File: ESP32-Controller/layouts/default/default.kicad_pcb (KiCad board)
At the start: 2 copper layers, 50 x 30 mm, 25 parts

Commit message: PoE Improvements
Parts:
- added C10: 10µF ±10%, Samsung_Electro_Mechanics_CL10A106KP8NNNC:C0603, F.Cu at (126.8, 101.1)
- added C11: 22µF ±20%, Samsung_Electro_Mechanics_CL10A226MQ8NRNC:C0603, F.Cu at (116.4, 95.5)
- added R7: 5.1kΩ ±1%, UNI_ROYAL_0402WGF5101TCE:R0402, F.Cu at (118.8, 92.4)
- added R8: 5.1kΩ ±1%, UNI_ROYAL_0402WGF5101TCE:R0402, F.Cu at (118.2, 88.3)
- added U2: , Advanced_Monolithic_Systems_AMS1117_3_3:SOT-223-3_L6.5-W3.4-P2.30-LS7.0-BR, F.Cu at (120.8, 100.6)
- R2: value 40.2kΩ ±1% -> 22kΩ ±1%; footprint UNI_ROYAL_0603WAF4022T5E:R0603 -> UNI_ROYAL_0603WAF2202T5E:R0603
- USB1: footprint Hanbo_Electronic_MC_401L68_Z09:USB-C-SMD_MC-401L68-Z09 -> Shenzhen_Kinghelm_Elec_KH_TYPE_C_16P:USB-C-SMD_KH-TYPE-C-16P
- moved USB1 8.31 mm to (123.4, 90.3), turned to 90 degrees
- moved D1 8.27 mm to (111.2, 85.1)
- moved C1 7.40 mm to (105.4, 101.0), turned to -90 degrees
- moved C2 4.80 mm to (98.8, 100.5), turned to 90 degrees
- moved 15V-25V DC 4.12 mm to (117.4, 82.6)
- moved C3 3.89 mm to (96.6, 100.5), turned to 90 degrees
- moved U1 0.30 mm to (102.2, 101.0), turned to 180 degrees
- renumbered SW1 to BOOT, SW2 to RESET
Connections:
- net A renamed BOOT
- net en_cap-power-hv renamed RESET
- D1 pad 1: V+ -> 5V
- L1 pad 2: 3V3 -> 5V
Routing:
- net 5V: track 0.00 -> 41.1 mm, vias 0 -> 3
- net V+: track 93.7 -> 62.6 mm
- net 3V3: track 56.4 -> 71.0 mm, vias 2 -> 0
- net lv: track 19.9 -> 8.04 mm
- net USB_Vin: track 12.9 -> 17.0 mm
- net GND: track 0.00 -> 3.08 mm, vias 10 -> 11
- net B5: track 0.00 -> 2.47 mm
- net A5: track 0.00 -> 2.38 mm
- net bst_cap-power-hv: track 3.40 -> 2.12 mm
- net fb_cap-power-lv: track 15.3 -> 16.6 mm, vias 0 -> 2
- net BOOT: track 12.7 -> 13.7 mm
- net A7: track 13.2 -> 13.8 mm
- net pwm_warm: vias 1 -> 2
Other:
- board size 50 x 30 mm -> 53.8 x 30 mm

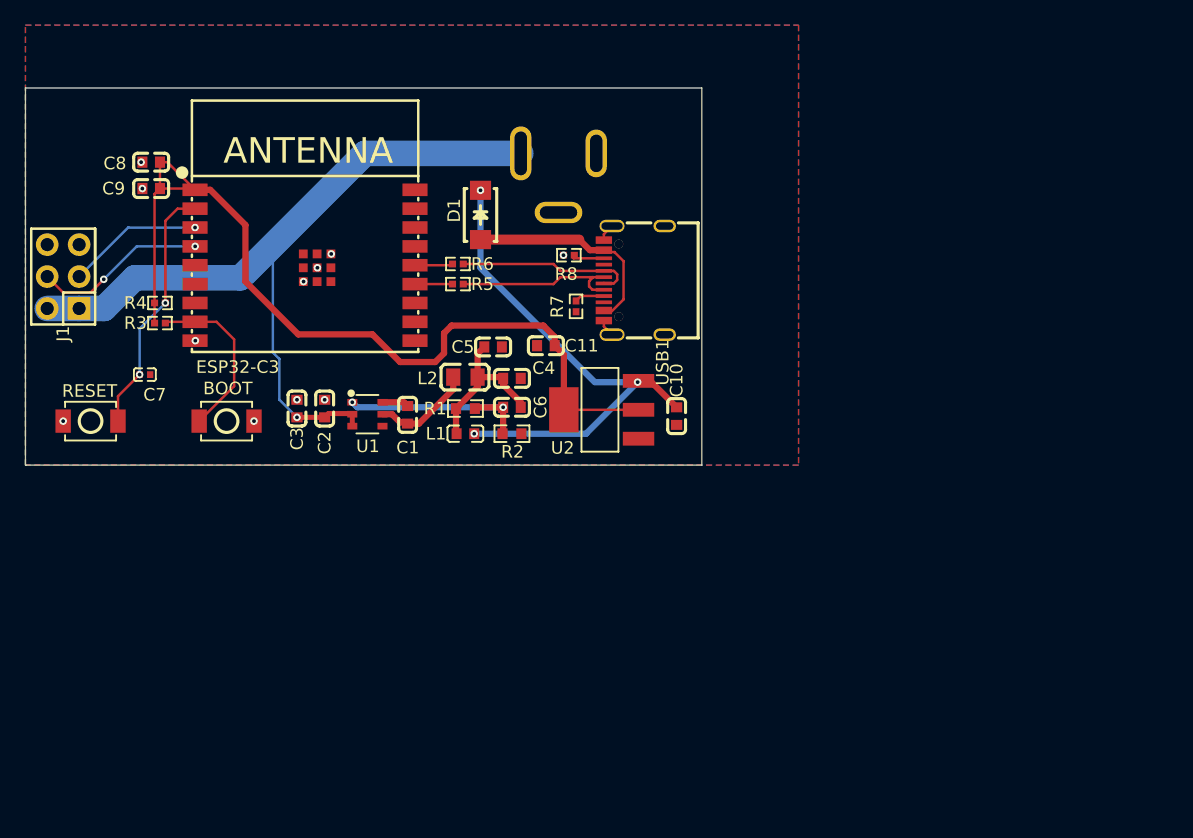
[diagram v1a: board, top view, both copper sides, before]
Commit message: ESP32 New Buck & Header Updates
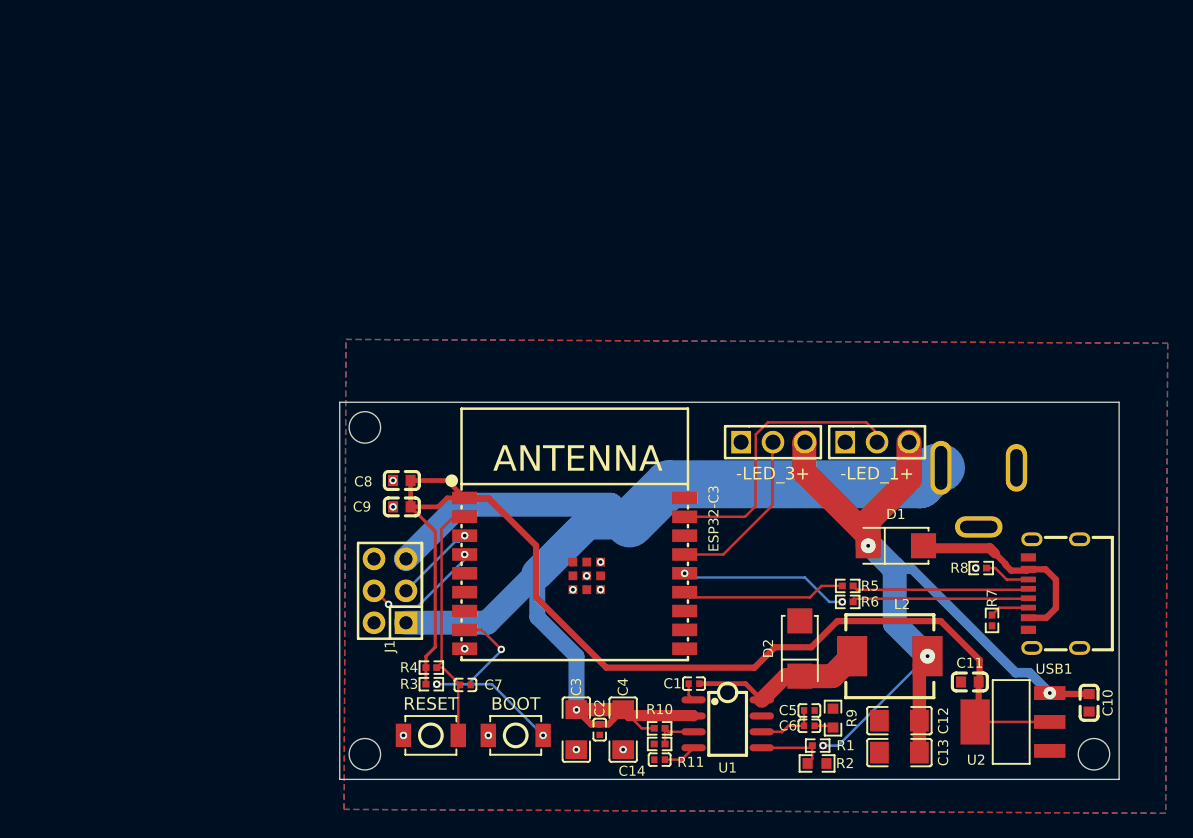
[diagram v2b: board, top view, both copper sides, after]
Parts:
- removed L1: , Murata_Electronics_BLM18PG121SN1D:L0603
- added -LED_1+: , BOOMELE_2_54_1_3P:HDR-TH_3P-P2.54-V-M-1, F.Cu at (142.7, 103.2)
- added -LED_3+: , BOOMELE_2_54_1_3P:HDR-TH_3P-P2.54-V-M-1, F.Cu at (134.5, 103.2)
- added C12: 47µF ±20%, Samsung_Electro_Mechanics_CL31A476MPHNNNE:C1206, F.Cu at (144.5, 125.3)
- added C13: 47µF ±20%, Samsung_Electro_Mechanics_CL31A476MPHNNNE:C1206, F.Cu at (144.5, 127.9)
- added C14: 10nF ±10%, Samsung_Electro_Mechanics_CL05B103KB5NNNC:C0402, F.Cu at (125.4, 128.4)
- added D2: Vf {ℝ+}V, MDD_Microdiode_Electronics_SS34:SMA_L4.3-W2.6-LS5.2-RD, F.Cu at (136.6, 119.6)
- added R10: 330kΩ ±1%, UNI_ROYAL_0402WGF3303TCE:R0402, F.Cu at (125.4, 125.9)
- added R11: 68kΩ ±1%, UNI_ROYAL_0402WGF6802TCE:R0402, F.Cu at (125.4, 127.2)
- added R9: 30kΩ ±1%, UNI_ROYAL_0603WAF3002T5E:R0603, F.Cu at (139.2, 125.1)
- C1: footprint YAGEO_CC0603KRX7R9BB104:C0603 -> Samsung_Electro_Mechanics_CL05B104KO5NNNC:C0402
- C10, C8: value 10µF ±10% -> 10µF ±20%
- C2: value 100nF ±10% -> 10nF ±10%; footprint YAGEO_CC0603KRX7R9BB104:C0603 -> Samsung_Electro_Mechanics_CL05B103KB5NNNC:C0402
- C3: value 10µF ±10% -> 4.7µF ±20%; footprint Samsung_Electro_Mechanics_CL10A106KP8NNNC:C0603 -> FH_1206B475K500NT:C1206
- C4: value 22µF ±20% -> 4.7µF ±20%; footprint Samsung_Electro_Mechanics_CL10A226MQ8NRNC:C0603 -> FH_1206B475K500NT:C1206
- C5: value 22µF ±20% -> 47pF ±5%; footprint Samsung_Electro_Mechanics_CL10A226MQ8NRNC:C0603 -> FH_0402CG470J500NT:C0402
- C6: value 47pF ±5% -> 1nF ±10%; footprint Samsung_Electro_Mechanics_CL10C470JB8NNNC:C0603 -> FH_0402B102K500NT:C0402
- C7: value 1µF ±10% -> 1µF ±20%
- C9: value 100nF ±10% -> 100nF ±20%
- D1: footprint MDD_Microdiode_Electronics_SS14:SMA_L4.2-W2.6-LS5.0-RD_1 -> MDD_Microdiode_Electronics_SS34:SMA_L4.3-W2.6-LS5.2-RD
- L2: footprint microgate_MGFL2012F6R8MT_LF:L0805 -> TECHFUSE_SL0630_6R8M:IND-SMD_L7.0-W6.6
- R1: value 120kΩ ±1% -> {ℝ+}Ω; footprint UNI_ROYAL_0603WAF1203T5E:R0603 -> UNI_ROYAL_0402WGF1002TCE:R0402
- R2: value 22kΩ ±1% -> {ℝ+}Ω; footprint UNI_ROYAL_0603WAF2202T5E:R0603 -> UNI_ROYAL_0603WAF1801T5E:R0603
- R3, R4: value 10kΩ ±1% -> 10kΩ ±5%
- R5, R6: value 22Ω ±1% -> 22Ω ±5%
- R7, R8: value 5.1kΩ ±1% -> 5.1kΩ ±5%
- U1: footprint Diodes_Incorporated_AP63301WU_7:TSOT-23-6_L2.9-W1.6-P0.95-LS2.8-BR -> Texas_Instruments_TPS54331DR:SOIC-8_L5.0-W4.0-P1.27-LS6.0-BL
- USB1: footprint Shenzhen_Kinghelm_Elec_KH_TYPE_C_16P:USB-C-SMD_KH-TYPE-C-16P -> Hanbo_Electronic_MC_403L68_Z20:USB-C-SMD_MC-403L68-Z20
- moved C11 43.0 mm to (150.1, 122.3)
- moved D1 42.2 mm to (144.2, 111.4), turned to 0 degrees
- moved 15V-25V DC 41.8 mm to (150.8, 107.6)
- moved USB1 41.7 mm to (156.8, 115.2)
- moved R7 41.5 mm to (151.9, 117.4)
- moved R8 41.2 mm to (151.0, 113.2)
- moved U2 41.1 mm to (153.5, 125.4)
- moved R6 41.0 mm to (140.4, 115.9)
- moved L2 40.4 mm to (143.8, 120.2)
- moved C10 40.0 mm to (159.6, 123.9)
- moved R5 39.2 mm to (140.4, 114.6)
- moved R1 38.8 mm to (138.0, 127.3), turned to 180 degrees
- moved C5 38.3 mm to (137.4, 124.5)
- moved U1 37.8 mm to (130.9, 125.6), turned to -90 degrees
- moved RESET 36.8 mm to (107.2, 126.5)
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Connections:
- net A5 renamed CC1
- net B5 renamed CC2
- C1 pad 1: bst_cap-power-hv -> hv
- C1 pad 2: lv -> cathode
- C4 pad 1: hv -> V+
- C5 pad 1: hv -> comp_c2-power-hv
- C6 pad 1: hv -> comp_c2-power-hv
- C6 pad 2: fb_cap-power-lv -> lv
- D1 pad 2: USB_Vin -> vUSB
- ESP32-C3 pad 15: 15 -> 2-1
- ESP32-C3 pad 17: 17 -> 2
- J1 pad 2: V+ -> GND
- J1 pad 5: GND -> V+
- L2 pad 1: lv -> cathode
- L2 pad 2: hv -> 5V
- R1 pad 1: hv -> 5V
- R1 pad 2: fb_cap-power-lv -> VSENSE
- R2 pad 1: fb_cap-power-lv -> VSENSE
- R5 pad 1: A7 -> usb_n
- R6 pad 1: A6 -> usb_p
- U1 pad 1: fb_cap-power-lv -> hv
- U1 pad 3: V+ -> EN
- U1 pad 4: GND -> ss_cap-power-hv
- U1 pad 5: lv -> VSENSE
- U1 pad 6: bst_cap-power-hv -> comp_c2-power-hv
- USB1 pad A6: A6 -> usb_p
- USB1 pad A7: A7 -> usb_n
- USB1 pad B4: USB_Vin -> vUSB
- USB1 pad B9: USB_Vin -> vUSB
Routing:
- net V+: track 62.6 -> 97.3 mm
- net 5V: track 41.1 -> 68.7 mm, vias 3 -> 4
- net 2: track 0.00 -> 22.0 mm
- net 3V3: track 71.0 -> 89.6 mm
- net USB_Vin: track 17.0 -> 0.00 mm
- net vUSB: track 0.00 -> 16.8 mm
- net fb_cap-power-lv: track 16.6 -> 0.00 mm, vias 2 -> 0
- net 2-1: track 0.00 -> 14.4 mm
- net A6: track 14.2 -> 0.00 mm
- net cathode: track 0.00 -> 14.1 mm
- net usb_n: track 0.00 -> 14.1 mm
- net usb_p: track 0.00 -> 14.0 mm
- net A7: track 13.8 -> 0.00 mm
- net hv: track 12.8 -> 1.45 mm
- net 14: track 3.02 -> 13.7 mm, vias 0 -> 2
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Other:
- board size 53.8 x 30 mm -> 62 x 30 mm

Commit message: Header & Silkscreen Updates
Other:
- board text added: "ESP32 LED Panel Controller v1.1.0 - May 2026"

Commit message: Basic layout tweaks
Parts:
- moved -LED_3+ 2.22 mm to (132.2, 103.2)
- moved -LED_1+ 0.50 mm to (142.2, 103.2)
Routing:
- net 2-1: track 14.4 -> 12.7 mm
- net 5V: track 68.7 -> 70.1 mm
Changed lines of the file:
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@@
 	(footprint "BOOMELE_2_54_1_3P:HDR-TH_3P-P2.54-V-M-1"
 		(layer "F.Cu")
-		(at 142.748 103.1748)
+		(at 142.25 103.1748)
 		(property "Reference" "-LED_1+"
 			(at 0 2.5 0)
@@
 	(footprint "BOOMELE_2_54_1_3P:HDR-TH_3P-P2.54-V-M-1"
 		(layer "F.Cu")
-		(at 134.4676 103.1748)
+		(at 132.25 103.1748)
 		(property "Reference" "-LED_3+"
 			(at 0 2.5 0)
@@
 	)
 	(segment
-		(start 133.096 108.2548)
-		(end 133.096 102.5652)
+		(start 127.4416 109.1096)
+		(end 129.3904 109.1096)
 		(width 0.2)
 		(layer "F.Cu")
@@
 	)
 	(segment
-		(start 133.096 102.5652)
-		(end 134.0612 101.6)
+		(start 141.8844 101.6)
+		(end 142.25 101.9656)
 		(width 0.2)
 		(layer "F.Cu")
@@
 	)
 	(segment
-		(start 134.0612 101.6)
+		(start 129.3904 109.1096)
+		(end 131 107.5)
+		(width 0.2)
+		(layer "F.Cu")
+		(net 30)
+	)
+	(segment
+		(start 131.9 101.6)
 		(end 141.8844 101.6)
 		(width 0.2)
@@
 	)
 	(segment
-		(start 141.8844 101.6)
-		(end 142.6972 102.4128)
+		(start 131 102.5)
+		(end 131.9 101.6)
 		(width 0.2)
 		(layer "F.Cu")
@@
 	)
 	(segment
-		(start 127.4416 109.1096)
-		(end 132.2412 109.1096)
+		(start 131 107.5)
+		(end 131 102.5)
 		(width 0.2)
 		(layer "F.Cu")
@@
 	)
 	(segment
-		(start 132.2412 109.1096)
-		(end 133.096 108.2548)
+		(start 142.25 101.9656)
+		(end 142.25 103.1748)
 		(width 0.2)
 		(layer "F.Cu")
@@
 	)
 	(segment
-		(start 134.4168 108.204)
-		(end 134.4168 102.4128)
+		(start 130.5112 112.1096)
+		(end 132.25 110.3708)
 		(width 0.2)
 		(layer "F.Cu")
@@
 	)
 	(segment
-		(start 130.5112 112.1096)
-		(end 134.4168 108.204)
+		(start 132.25 110.3708)
+		(end 132.25 103.1748)
 		(width 0.2)
 		(layer "F.Cu")
@@
 	)
 	(segment
-		(start 142.0404 110.646)
-		(end 136.9568 105.5624)
-		(width 1.905)
-		(layer "F.Cu")
-		(net 32)
-	)
-	(segment
 		(start 156.8584 123.1316)
 		(end 156.9344 123.2076)
@@
 	)
 	(segment
+		(start 134.75 103.2148)
+		(end 134.79 103.1748)
+		(width 1.905)
+		(layer "F.Cu")
+		(net 32)
+	)
+	(segment
 		(start 142.0404 111.416)
-		(end 142.0404 110.646)
+		(end 141.166 111.416)
 		(width 1.905)
 		(layer "F.Cu")
@@
 	)
 	(segment
-		(start 136.9568 103.2256)
-		(end 137.0076 103.1748)
+		(start 141.166 111.416)
+		(end 134.75 105)
 		(width 1.905)
 		(layer "F.Cu")
@@
 	)
 	(segment
-		(start 136.9568 105.5624)
-		(end 136.9568 103.2256)
+		(start 134.75 105)
+		(end 134.75 103.2148)
 		(width 1.905)
 		(layer "F.Cu")
@@
 		(polygon
 			(pts
-				(xy 100.5 95) (xy 165.8608 95.3048) (xy 165.7084 132.6924) (xy 100.3476 132.3876)
+				(xy 97.720501 94.987038) (xy 165.8608 95.3048) (xy 165.7084 132.6924) (xy 97.568101 132.374638)
 			)
 		)

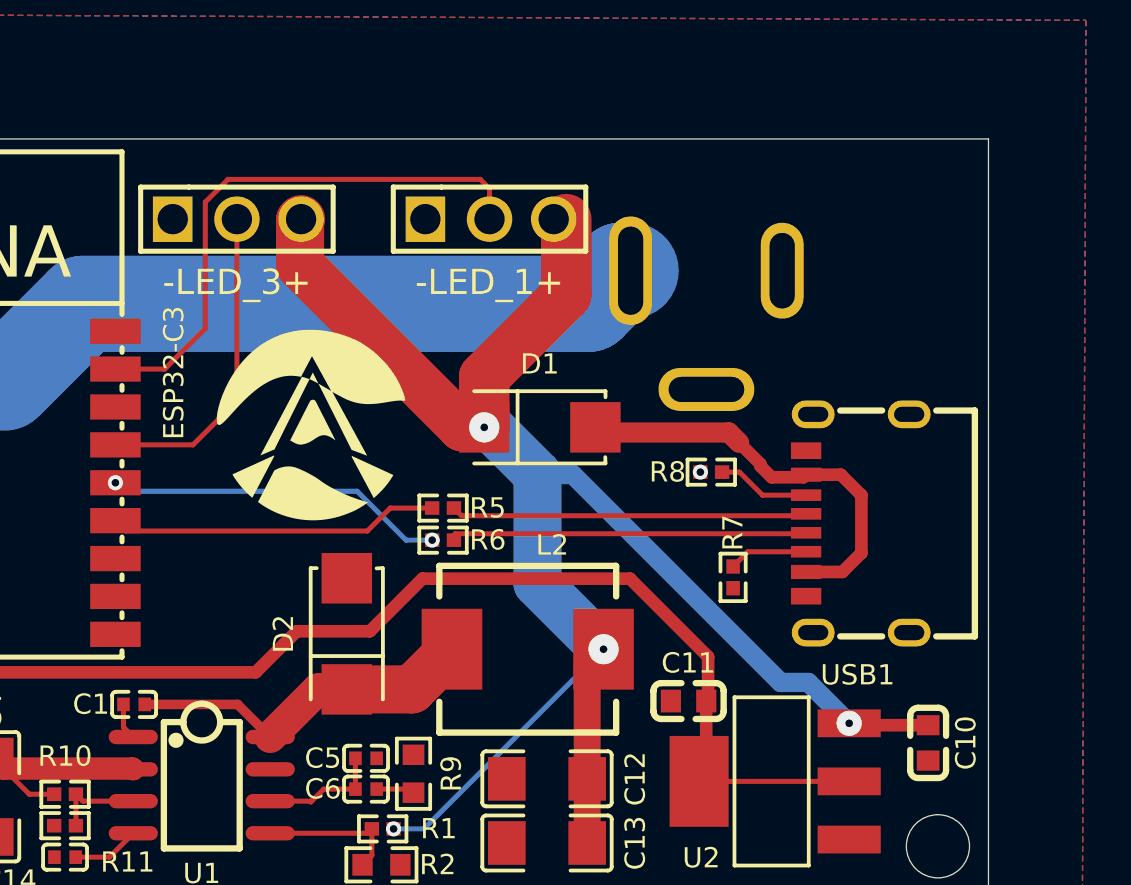
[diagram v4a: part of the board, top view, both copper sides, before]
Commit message: Fixed 3D offsets, flipped some DC jacks, and added screw holes
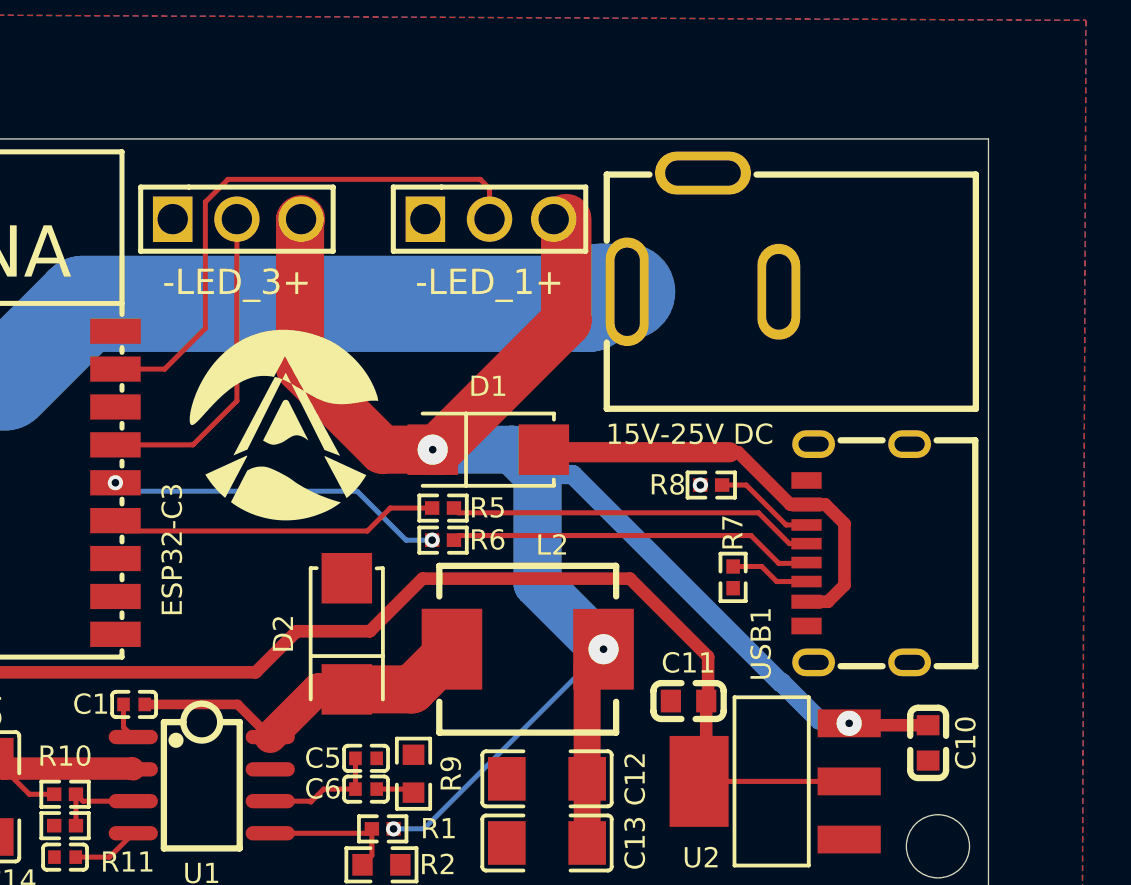
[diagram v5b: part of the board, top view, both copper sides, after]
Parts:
- added QR*****: LED-GitHub-QR-MD, Silkscreen:LED-GitHub-QR-MD, B.Cu at (139.6, 110.0)
- added REF**: OSHW-Logo2_7.3x6mm_SilkScreen, Symbol:OSHW-Logo2_7.3x6mm_SilkScreen, B.Cu at (139.2, 121.9)
- added REF**: KiCad-Logo2_5mm_SilkScreen, Symbol:KiCad-Logo2_5mm_SilkScreen, B.Cu at (150.5, 121.4)
- 15V-25V DC: moved to F.Cu
- moved 15V-25V DC 3.87 mm to (150.7, 103.7)
- moved D1 2.22 mm to (142.2, 112.3)
- moved USB1 1.18 mm to (156.8, 116.4)
- moved R8 0.51 mm to (151.0, 113.7)
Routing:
- net 5V: track 70.1 -> 74.4 mm
- net usb_p: track 14.0 -> 14.5 mm
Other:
- board text added: "ESP32 LED Panel Controller v1.1.1 - June 2026"
- board text removed: "ESP32 LED Panel Controller v1.1.0 - May 2026"
